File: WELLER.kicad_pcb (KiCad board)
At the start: 2 copper layers, 20 x 100 mm, 86 parts, among them J1 Jack-DC, J2 AudioJack3_Ground_SwitchR, J3 debug+programing, J4 I2c oled, Q1 AON7403, Q2 AON7403, Q3 AON7403, SW1 SW_Push_SPDT, SW2 SW_Push, SW3 SW_Push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

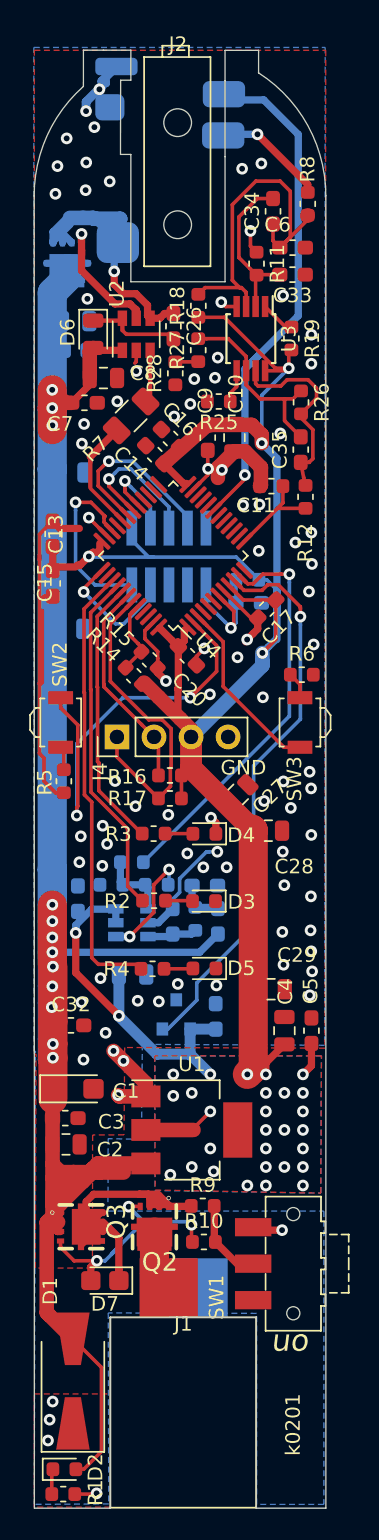
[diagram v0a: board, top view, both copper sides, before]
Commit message: update błędnego podpięcia pmosa na wejściu do układu, oras software testujący oled, przyciski i ledy
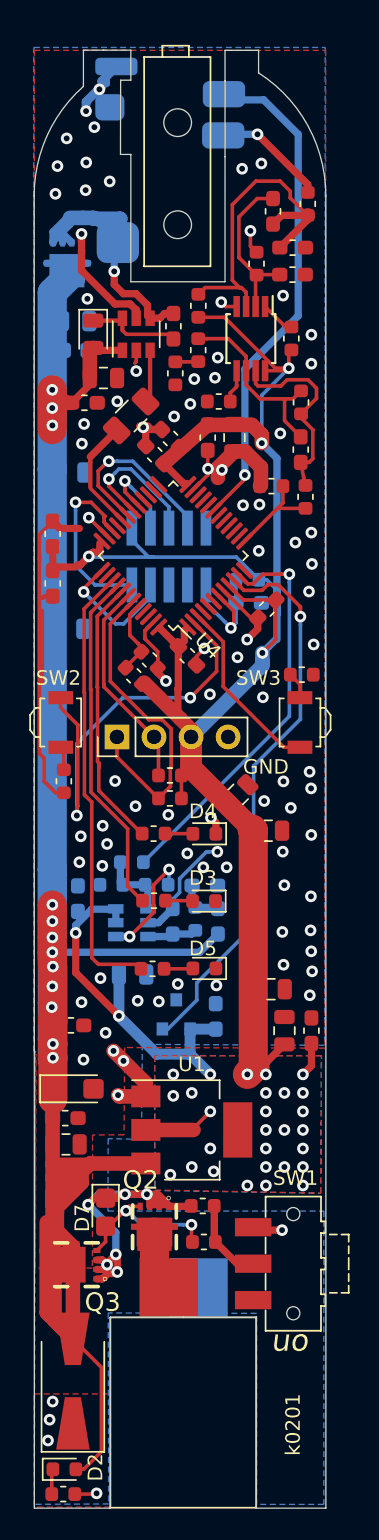
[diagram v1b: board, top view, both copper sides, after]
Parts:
- R14: value 10k -> NC
- moved D7 4.69 mm to (124.9, 104.7), turned to 270 degrees
- moved Q3 2.62 mm to (122.9, 108.3), turned to 90 degrees
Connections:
- Q3 pad 1: /tip_driving/12V -> Net-(D7-Pad1)
- Q3 pad 2: /tip_driving/12V -> Net-(D7-Pad1)
- Q3 pad 3: /tip_driving/12V -> Net-(D7-Pad1)
- Q3 pad 5: Net-(D7-Pad1) -> /tip_driving/12V
- Q3 pad 6: Net-(D7-Pad1) -> /tip_driving/12V
- Q3 pad 7: Net-(D7-Pad1) -> /tip_driving/12V
- Q3 pad 8: Net-(D7-Pad1) -> /tip_driving/12V
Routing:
- net /tip_driving/12V: track 149.9 -> 165.1 mm
- net Net-(D7-Pad2): track 16.5 -> 11.7 mm, vias 3 -> 2
- net GND: track 79.2 -> 82.3 mm, vias 88 -> 89
- net Net-(D7-Pad1): track 30.7 -> 29.5 mm, vias 0 -> 6
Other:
- board text added: "3.3v"
- board text added: "NSRT"
- board text added: "SCL"
- board text added: "SDA"
- board text added: "SWCLK"
- board text added: "SWDIO"
- board text added: "USART CLK"
- board text added: "USART RX"
- board text added: "USART TX"
